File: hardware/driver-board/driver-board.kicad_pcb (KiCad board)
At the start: 4 copper layers, 111.8 x 69.8 mm, 71 parts, among them J1 Conn_ARM_JTAG_SWD_10, J2 USB_C_Receptacle_USB2.0_16P, J3 CONN_MOTOR_R, J4 CONN_MOTOR_L, Q1 AO3401A, Q2 AO4407A, SW1 SW_Push, SW2 SK-3296S-01-L2, U1 STM32F103CBT6, U2 USBLC6-2SC6, U3 DRV8838, U4 DRV8838, U5 LMR51430XDDCR, Y1 16Mhz

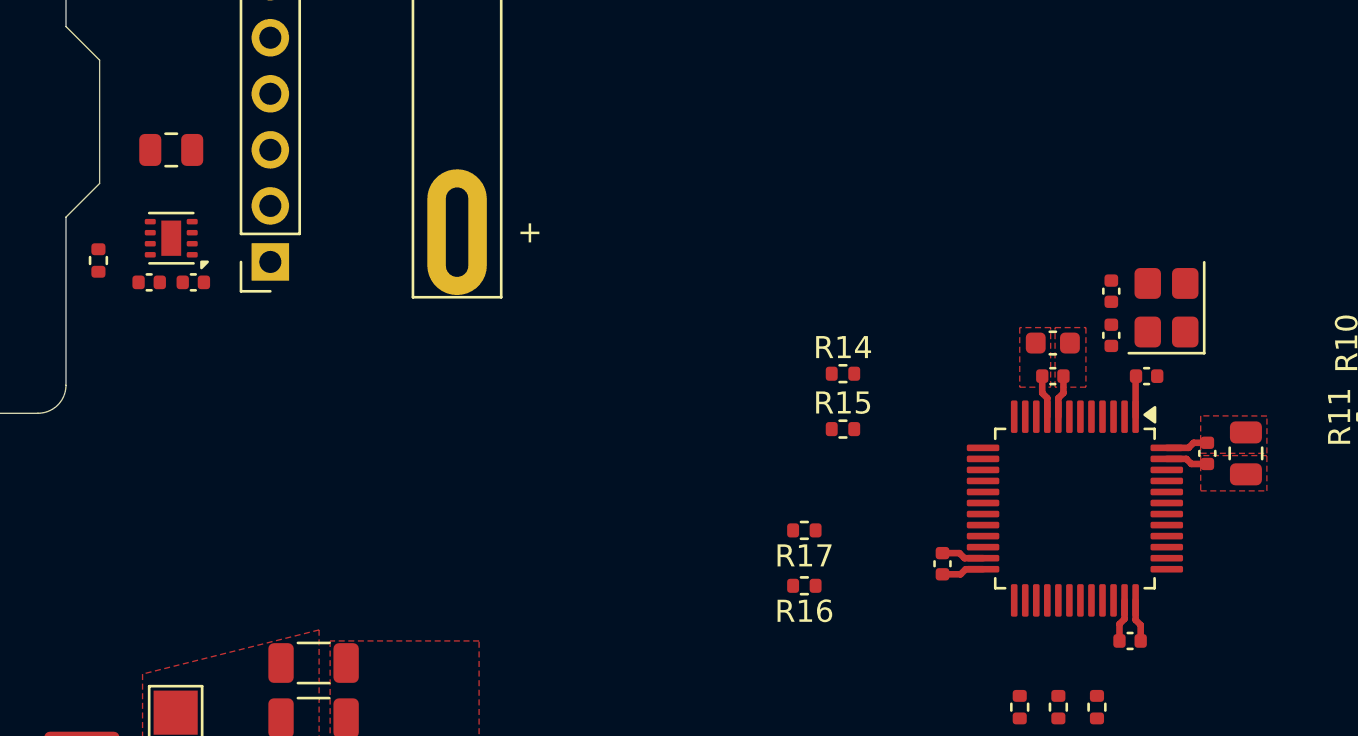
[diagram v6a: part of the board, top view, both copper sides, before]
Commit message: Route MCU oscillator and improve grounding
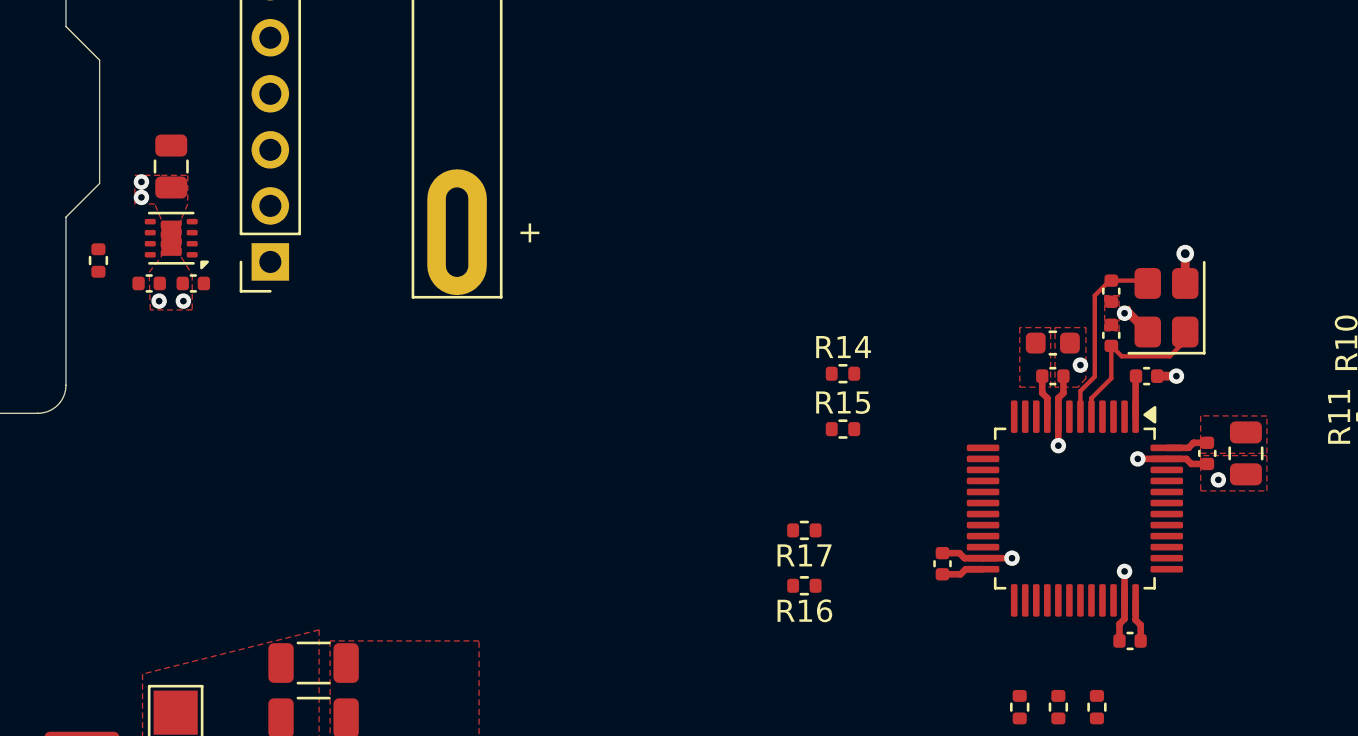
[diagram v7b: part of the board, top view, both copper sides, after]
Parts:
- moved C10 0.75 mm to (59.0, 92.5), turned to -90 degrees
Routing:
- net GND: track 7.73 -> 16.6 mm, vias 0 -> 13
- net /HSE_OUT: track 0.00 -> 8.49 mm
- net /HSE_IN: track 0.00 -> 7.81 mm

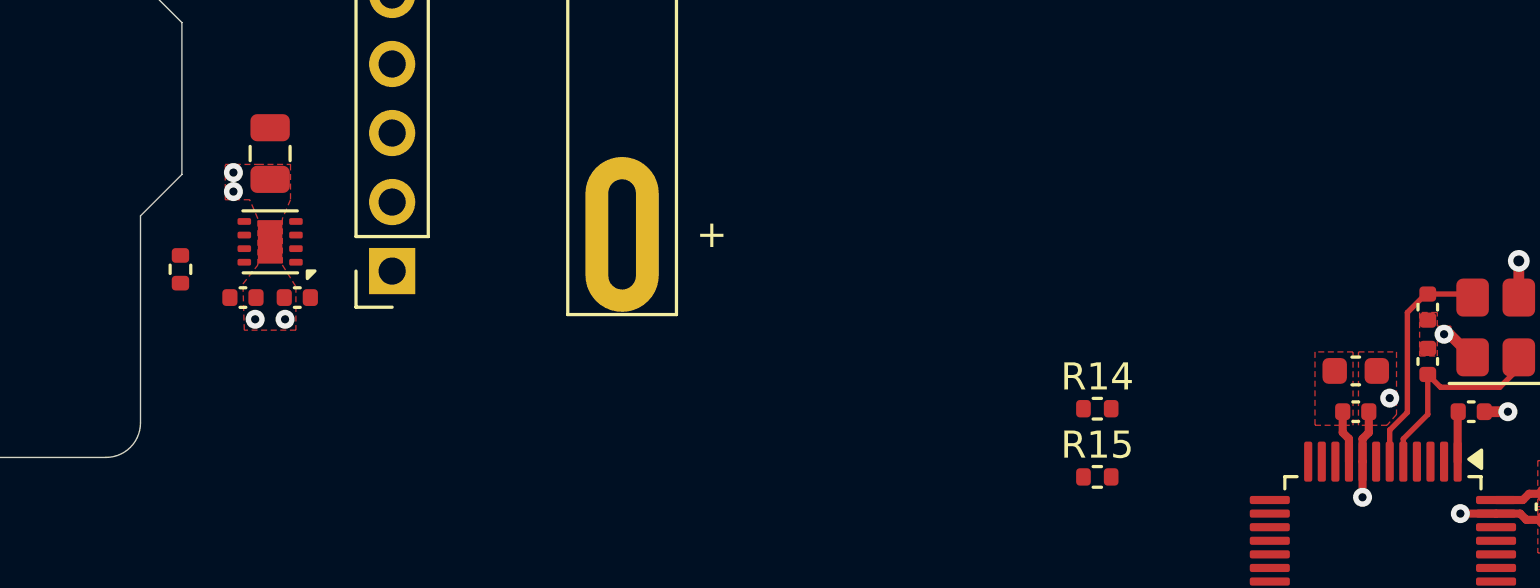
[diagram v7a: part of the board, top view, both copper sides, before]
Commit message: Add VDDA supply filter
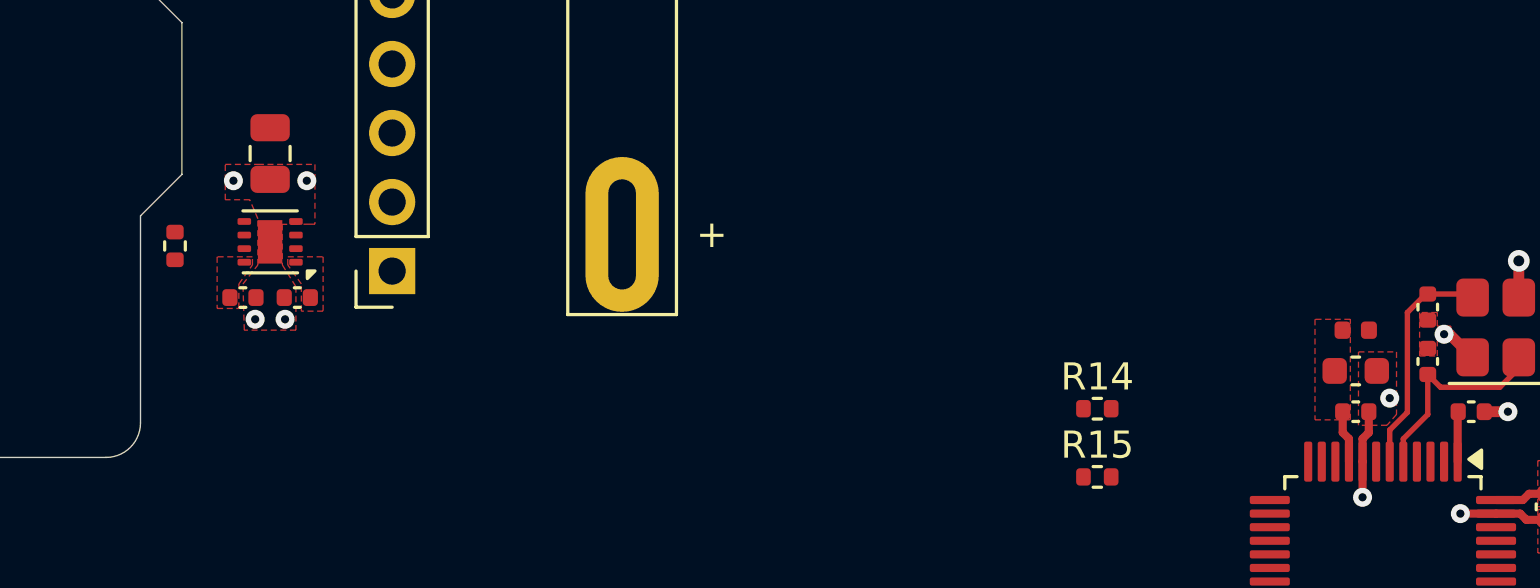
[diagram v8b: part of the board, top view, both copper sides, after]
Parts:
- added L2: 39n, Inductor_SMD:L_0402_1005Metric, F.Cu at (99.0, 99.0)
- moved R12 0.88 mm to (55.5, 95.9)
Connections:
- C22 pad 1: +3V3 -> +3V3A
- C23 pad 1: +3V3 -> +3V3A
- U1 pad 9: +3V3 -> +3V3A
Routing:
- net +3V3A: track 0.00 -> 1.93 mm
- net +3V3: track 9.58 -> 7.64 mm
- added copper zone on F.Cu, net +3V3A
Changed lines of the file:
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@@
 		(embedded_fonts no)
 	)
+	(footprint "Inductor_SMD:L_0402_1005Metric"
+		(layer "F.Cu")
+		(at 99 99)
+		(descr "Inductor SMD 0402 (1005 Metric), square (rectangular) end terminal, IPC-7351 nominal, (Body size source: http://www.tortai-tech.com/upload/download/2011102023233369053.pdf)")
+		(tags "inductor")
+		(property "Reference" "L2"
+			(at 0 -1.17 0)
+			(layer "F.Fab")
+			(effects
+				(font
+					(size 1 1)
+					(thickness 0.15)
+				)
+			)
+		)
+		(property "Value" "39n"
+			(at 0 1.17 0)
+			(layer "F.Fab")
+			(effects
+				(font
+					(size 1 1)
+					(thickness 0.15)
+				)
+			)
+		)
+		(property "Datasheet" ""
+			(at 0 0 0)
+			(layer "F.Fab")
+			(hide yes)
+			(effects
+				(font
+					(size 1.27 1.27)
+				)
+			)
+		)
+		(property "Description" "STM32F103 VDDA series filter inductor: 39 nH, 0402; place between +3V3 and +3V3A immediately beside C22/C23 and U1 pin 9"
+			(at 0 0 0)
+			(layer "F.Fab")
+			(hide yes)
+			(effects
+				(font
+					(size 1.27 1.27)
+				)
+			)
+		)
+		(property "KiLib_Generator" "SMD_2terminal_chip_molded"
+			(at 0 0 0)
+			(layer "F.SilkS")
+			(hide yes)
+			(effects
+				(font
+					(size 1 1)
+					(thickness 0.15)
+				)
+			)
+		)
+		(property "JLCPCB" ""
+			(at 0 0 0)
+			(unlocked yes)
+			(layer "F.Fab")
+			(hide yes)
+			(effects
+				(font
+					(size 1 1)
+					(thickness 0.15)
+				)
+			)
+		)
+		(property ki_fp_filters "Choke_* *Coil* Inductor_* L_*")
+		(sheetname "/")
+		(sheetfile "driver-board.kicad_sch")
+		(units
+			(unit
+				(name "A")
+				(pins "1" "2")
+			)
+		)
+		(attr smd)
+		(duplicate_pad_numbers_are_jumpers no)
+		(fp_rect
+			(start -0.93 -0.47)
+			(end 0.93 0.47)
+			(stroke
+				(width 0.05)
+				(type solid)
+			)
+			(fill no)
+			(layer "F.CrtYd")
+		)
+		(fp_rect
+			(start -0.5 -0.25)
+			(end 0.5 0.25)
+			(stroke
+				(width 0.1)
+				(type solid)
+			)
+			(fill no)
+			(layer "F.Fab")
+		)
+		(fp_text user "${REFERENCE}"
+			(at 0 0 0)
+			(layer "F.Fab")
+			(effects
+				(font
+					(size 0.25 0.25)
+					(thickness 0.04)
+				)
+			)
+		)
+		(pad "1" smd roundrect
+			(at -0.485 0)
+			(size 0.59 0.64)
+			(layers "F.Cu" "F.Mask" "F.Paste")
+			(roundrect_rratio 0.25)
+			(net "+3V3A")
+			(pintype "passive")
+		)
+		(pad "2" smd roundrect
+			(at 0.485 0)
+			(size 0.59 0.64)
+			(layers "F.Cu" "F.Mask" "F.Paste")
+			(roundrect_rratio 0.25)
+			(net "+3V3")
+			(pintype "passive")
+		)
+		(embedded_fonts no)
+		(model "${KICAD10_3DMODEL_DIR}/Inductor_SMD.3dshapes/L_0402_1005Metric.step"
+			(offset
+				(xyz 0 0 0)
+			)
+			(scale
+				(xyz 1 1 1)
+			)
+			(rotate
+				(xyz 0 0 0)
+			)
+		)
+	)
 	(footprint "Resistor_SMD:R_0402_1005Metric"
 		(layer "F.Cu")
@@
 	(footprint "Resistor_SMD:R_0402_1005Metric"
 		(layer "F.Cu")
-		(at 55.75 96.76 90)
+		(at 55.55 95.9 90)
 		(descr "Resistor SMD 0402 (1005 Metric), square (rectangular) end terminal, IPC-7351 nominal, (Body size source: IPC-SM-782 page 72, https://www.pcb-3d.com/wordpress/wp-content/uploads/ipc-sm-782a_amendment_1_and_2.pdf)")
 		(tags "resistor")
@@
 			(layers "F.Cu" "F.Mask" "F.Paste")
 			(roundrect_rratio 0.25)
-			(net "+3V3")
+			(net "+3V3A")
 			(pinfunction "VDDA_9")
 			(pintype "power_in")
@@
 			(layers "F.Cu" "F.Mask" "F.Paste")
 			(roundrect_rratio 0.25)
-			(net "+3V3")
+			(net "+3V3A")
 			(pintype "passive")
 		)
@@
 			(layers "F.Cu" "F.Mask" "F.Paste")
 			(roundrect_rratio 0.25)
-			(net "+3V3")
+			(net "+3V3A")
 			(pintype "passive")
 		)
@@
 	)
 	(via
-		(at 57.7 93.9)
+		(at 57.7 93.5)
 		(size 0.7)
 		(drill 0.3)
@@
 	)
 	(via
-		(at 57.7 93.2)
+		(at 60.4 93.5)
 		(size 0.7)
 		(drill 0.3)
@@
 	)
 	(segment
-		(start 98.52 102.76688)
-		(end 98.52 102)
-		(width 0.3)
-		(layer "F.Cu")
-		(net "+3V3")
-	)
-	(segment
 		(start 102.75 113.05)
 		(end 102.98 113.28)
@@
 	)
 	(segment
-		(start 98.75 102.99688)
-		(end 98.52 102.76688)
-		(width 0.3)
-		(layer "F.Cu")
-		(net "+3V3")
-	)
-	(segment
 		(start 95.05 110.75)
 		(end 94.82 110.98)
@@
 	)
 	(segment
-		(start 98.75 103.8375)
-		(end 98.75 102.99688)
-		(width 0.3)
-		(layer "F.Cu")
-		(net "+3V3")
-	)
-	(segment
 		(start 105.15 105.25)
 		(end 105.38 105.02)
@@
 	)
 	(segment
+		(start 98.52 102.76688)
+		(end 98.52 102)
+		(width 0.3)
+		(layer "F.Cu")
+		(net "+3V3A")
+	)
+	(segment
+		(start 98.75 102.99688)
+		(end 98.52 102.76688)
+		(width 0.3)
+		(layer "F.Cu")
+		(net "+3V3A")
+	)
+	(segment
+		(start 98.75 103.8375)
+		(end 98.75 102.99688)
+		(width 0.3)
+		(layer "F.Cu")
+		(net "+3V3A")
+	)
+	(segment
 		(start 72.00304 96.99696)
 		(end 72.00304 95.47626)
@@
 	)
 	(zone
-		(net "+3V3")
+		(net "GND")
 		(layer "F.Cu")
 		(hatch edge 0.5)
-		(priority 7)
+		(priority 6)
 		(connect_pads yes
 			(clearance 0.3)
@@
 		(polygon
 			(pts
-				(xy 98.9 102.5) (xy 98.9 99.8) (xy 97.5 99.8) (xy 97.5 102.5)
+				(xy 100.5 99.8) (xy 100.5 102.1) (xy 100.15 102.5) (xy 99.1 102.5) (xy 99.1 99.8)
 			)
 		)
 	)
 	(zone
-		(net "GND")
+		(net "+3V3")
 		(layer "F.Cu")
 		(hatch edge 0.5)
-		(priority 6)
-		(connect_pads yes
-			(clearance 0.3)
+		(priority 2)
+		(connect_pads
+			(clearance 0.5)
 		)
 		(min_thickness 0.25)
@@
 		(polygon
 			(pts
-				(xy 100.5 99.8) (xy 100.5 102.1) (xy 100.15 102.5) (xy 99.1 102.5) (xy 99.1 99.8)
+				(xy 57.75 115.5) (xy 57.75 119.01785) (xy 61.75 127.25) (xy 65.75 127.25) (xy 65.75 113.5)
 			)
 		)
@@
 		(layer "F.Cu")
 		(hatch edge 0.5)
-		(priority 2)
-		(connect_pads
-			(clearance 0.5)
+		(priority 10)
+		(connect_pads yes
+			(clearance 0.3)
 		)
 		(min_thickness 0.25)
@@
 		(polygon
 			(pts
-				(xy 57.75 115.5) (xy 57.75 119.01785) (xy 61.75 127.25) (xy 65.75 127.25) (xy 65.75 113.5)
+				(xy 57.9 98.2) (xy 57.9 97.3) (xy 58.4 96.6) (xy 58.4 96.3) (xy 57.1 96.3) (xy 57.1 98.2)
 			)
 		)
@@
 	)
 	(zone
+		(net "+3V3A")
+		(layer "F.Cu")
+		(hatch edge 0.5)
+		(priority 7)
+		(connect_pads yes
+			(clearance 0.3)
+		)
+		(min_thickness 0.25)
+		(fill yes
+			(thermal_gap 0.5)
+			(thermal_bridge_width 0.5)
+			(island_removal_mode 0)
+		)
+		(polygon
+			(pts
+				(xy 98.8 102.3) (xy 98.8 98.6) (xy 97.5 98.6) (xy 97.5 102.3)
+			)
+		)
+	)
+	(zone
 		(net "VBAT_SW")
 		(layer "F.Cu")
@@
 	)
 	(zone
+		(net "VBAT_SW")
+		(layer "F.Cu")
+		(hatch edge 0.5)
+		(priority 11)
+		(connect_pads yes
+			(clearance 0.3)
+		)
+		(min_thickness 0.25)
+		(fill yes
+			(thermal_gap 0.5)
+			(thermal_bridge_width 0.5)
+			(island_removal_mode 0)
+		)
+		(polygon
+			(pts
+				(xy 61 98.3) (xy 60.2 98.3) (xy 60.2 97.3) (xy 59.7 96.6) (xy 59.7 96.3) (xy 61 96.3)
+			)
+		)
+	)
+	(zone
 		(net "GND")
 		(layer "F.Cu")
@@
 		(polygon
 			(pts
-				(xy 59.8 92.9) (xy 59.8 94.2) (xy 59.5 94.9) (xy 59.5 96.6) (xy 60 97.4) (xy 60 99) (xy 58.1 99)
-				(xy 58.05 97.3) (xy 58.6 96.6) (xy 58.6 94.9) (xy 58.3 94.2) (xy 57.4 94.2) (xy 57.4 92.9) (xy 58.6 92.9)
+				(xy 60.7 92.9) (xy 60.7 95.1) (xy 60.499288 95.099898) (xy 60.031813 95.103357) (xy 59.493749 95.105608)
+				(xy 59.5 96.6) (xy 60 97.4) (xy 60 99) (xy 58.1 99) (xy 58.05 97.3) (xy 58.6 96.6) (xy 58.6 94.9)
+				(xy 58.3 94.2) (xy 57.4 94.2) (xy 57.4 92.9) (xy 58.6 92.9)
 			)
 		)
